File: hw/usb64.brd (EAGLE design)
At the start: 68.6 x 62.5 mm, 22 parts

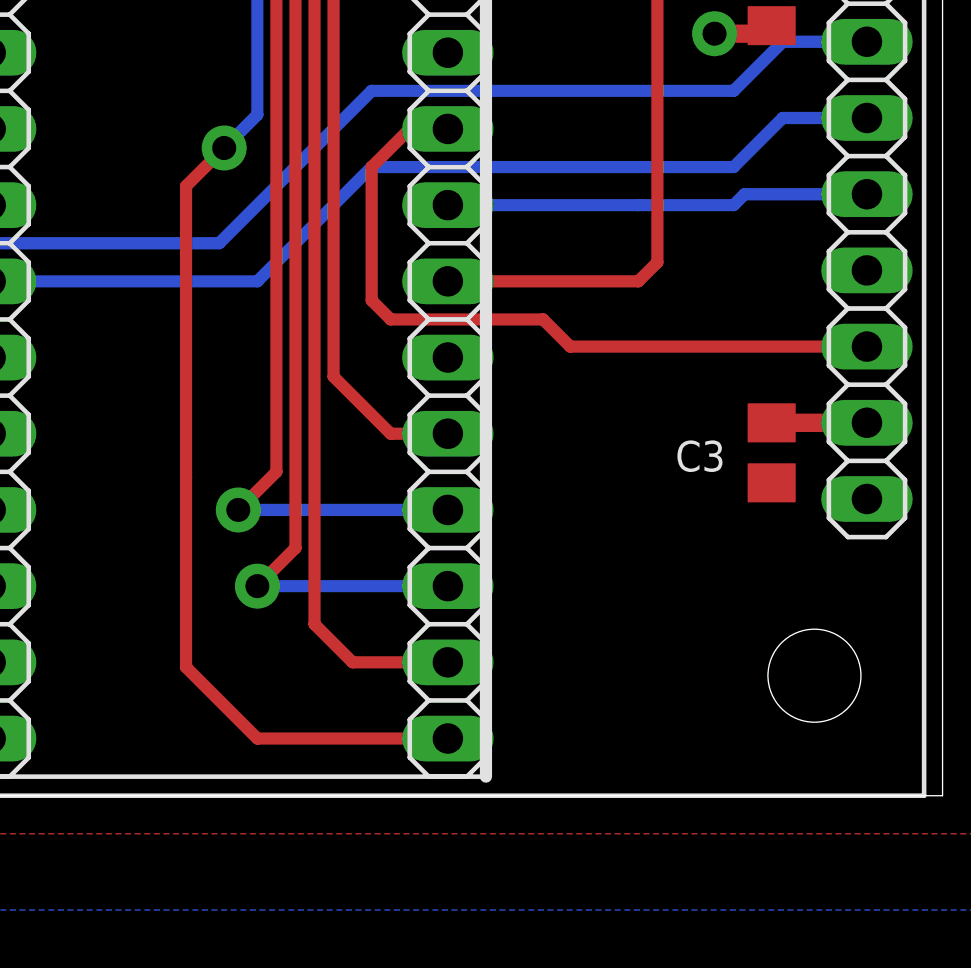
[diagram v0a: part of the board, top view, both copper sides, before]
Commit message: hw: Add 100pF filtering capacitors
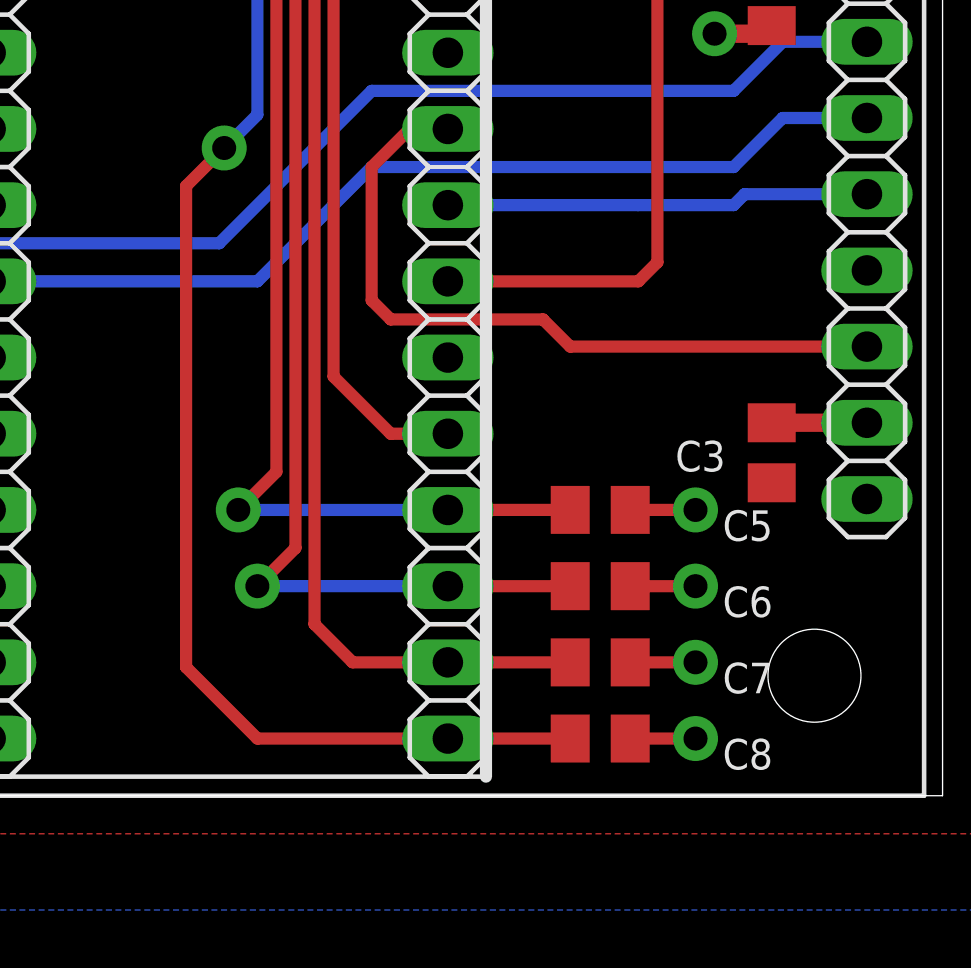
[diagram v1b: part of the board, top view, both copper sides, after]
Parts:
- added C5, C6, C7, C8: 100p, rcl:C0805K
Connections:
- net GND: now also C5.2, C6.2, C7.2, C8.2
- net N64_1: now also C5.1
- net N64_2: now also C6.1
- net N64_3: now also C7.1
- net N64_4: now also C8.1
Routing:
- net GND: track 26.6 -> 35.3 mm, vias 5 -> 9
- net N64_4: track 62.6 -> 66.7 mm
- net N64_3: track 62.9 -> 67.0 mm
- net N64_2: track 71.0 -> 75.1 mm
- net N64_1: track 76.3 -> 80.4 mm
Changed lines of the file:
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@@
 <attribute name="PURCHASE-URL" value="https://pricing.snapeda.com/search/part/USB-A1HSW6/?ref=eda" x="22.225" y="4.445" size="1.778" layer="27" display="off"/>
+</element>
+<element name="C5" library="rcl" library_urn="urn:adsk.eagle:library:334" package="C0805K" package3d_urn="urn:adsk.eagle:package:23681/2" value="100p" x="57.15" y="9.525" smashed="yes">
+<attribute name="NAME" x="61.23" y="8.495" size="1.016" layer="25"/>
+<attribute name="POPULARITY" value="52" x="57.15" y="9.525" size="1.778" layer="27" display="off"/>
+<attribute name="SPICEPREFIX" value="C" x="57.15" y="9.525" size="1.778" layer="27" display="off"/>
+</element>
+<element name="C6" library="rcl" library_urn="urn:adsk.eagle:library:334" package="C0805K" package3d_urn="urn:adsk.eagle:package:23681/2" value="100p" x="57.15" y="6.985" smashed="yes">
+<attribute name="NAME" x="61.23" y="5.955" size="1.016" layer="25"/>
+<attribute name="POPULARITY" value="52" x="57.15" y="6.985" size="1.778" layer="27" display="off"/>
+<attribute name="SPICEPREFIX" value="C" x="57.15" y="6.985" size="1.778" layer="27" display="off"/>
+</element>
+<element name="C7" library="rcl" library_urn="urn:adsk.eagle:library:334" package="C0805K" package3d_urn="urn:adsk.eagle:package:23681/2" value="100p" x="57.15" y="4.445" smashed="yes">
+<attribute name="NAME" x="61.23" y="3.415" size="1.016" layer="25"/>
+<attribute name="POPULARITY" value="52" x="57.15" y="4.445" size="1.778" layer="27" display="off"/>
+<attribute name="SPICEPREFIX" value="C" x="57.15" y="4.445" size="1.778" layer="27" display="off"/>
+</element>
+<element name="C8" library="rcl" library_urn="urn:adsk.eagle:library:334" package="C0805K" package3d_urn="urn:adsk.eagle:package:23681/2" value="100p" x="57.15" y="1.905" smashed="yes">
+<attribute name="NAME" x="61.23" y="0.875" size="1.016" layer="25"/>
+<attribute name="POPULARITY" value="52" x="57.15" y="1.905" size="1.778" layer="27" display="off"/>
+<attribute name="SPICEPREFIX" value="C" x="57.15" y="1.905" size="1.778" layer="27" display="off"/>
 </element>
 </elements>
@@
 <vertex x="78.74" y="72.39"/>
 </polygon>
+<contactref element="C6" pad="2"/>
+<contactref element="C7" pad="2"/>
+<contactref element="C8" pad="2"/>
+<contactref element="C5" pad="2"/>
+<wire x1="58.15" y1="9.525" x2="60.325" y2="9.525" width="0.4064" layer="1"/>
+<via x="60.325" y="9.525" extent="1-16" drill="0.8" diameter="1.5"/>
+<wire x1="58.15" y1="6.985" x2="60.325" y2="6.985" width="0.4064" layer="1"/>
+<via x="60.325" y="6.985" extent="1-16" drill="0.8" diameter="1.5"/>
+<wire x1="58.15" y1="4.445" x2="60.325" y2="4.445" width="0.4064" layer="1"/>
+<via x="60.325" y="4.445" extent="1-16" drill="0.8" diameter="1.5"/>
+<wire x1="58.15" y1="1.905" x2="60.325" y2="1.905" width="0.4064" layer="1"/>
+<via x="60.325" y="1.905" extent="1-16" drill="0.8" diameter="1.5"/>
 </signal>
 <signal name="N64_1">
@@
 <wire x1="6.35" y1="38.735" x2="24.765" y2="38.735" width="0.4064" layer="1"/>
 <wire x1="34.925" y1="28.575" x2="45.085" y2="28.575" width="0.4064" layer="1"/>
+<contactref element="C5" pad="1"/>
+<wire x1="56.15" y1="9.525" x2="52.07" y2="9.525" width="0.4064" layer="1"/>
 </signal>
 <signal name="N64_SENSE">
@@
 <via x="44.6144" y="21.59" extent="1-16" drill="0.8" diameter="1.5"/>
 <wire x1="44.6144" y1="21.59" x2="43.3444" y2="20.32" width="0.4064" layer="1"/>
-<wire x1="43.3444" y1="20.32" x2="43.3444" y2="10.61795625" width="0.4064" layer="1"/>
-<wire x1="43.3444" y1="10.61795625" x2="43.3444" y2="4.2806" width="0.4064" layer="1"/>
+<wire x1="43.3444" y1="20.32" x2="43.3444" y2="4.2806" width="0.4064" layer="1"/>
 <wire x1="43.3444" y1="4.2806" x2="45.72" y2="1.905" width="0.4064" layer="1"/>
 <wire x1="45.72" y1="1.905" x2="52.07" y2="1.905" width="0.4064" layer="1"/>
 <wire x1="45.72" y1="36.195" x2="45.72" y2="22.6956" width="0.4064" layer="16"/>
+<contactref element="C8" pad="1"/>
+<wire x1="52.07" y1="1.905" x2="56.15" y2="1.905" width="0.4064" layer="1"/>
 </signal>
 <signal name="N64_3">
@@
 <wire x1="25.87973125" y1="40.005" x2="32.22973125" y2="33.655" width="0.4064" layer="1"/>
 <wire x1="32.22973125" y1="33.655" x2="45.7962" y2="33.655" width="0.4064" layer="1"/>
+<contactref element="C7" pad="1"/>
+<wire x1="52.07" y1="4.445" x2="56.15" y2="4.445" width="0.4064" layer="1"/>
 </signal>
 <signal name="N64_2">
@@
 <wire x1="15.24" y1="39.37" x2="25.4" y2="39.37" width="0.4064" layer="1"/>
 <wire x1="33.655" y1="31.115" x2="45.72" y2="31.115" width="0.4064" layer="1"/>
+<contactref element="C6" pad="1"/>
+<wire x1="52.07" y1="6.985" x2="56.15" y2="6.985" width="0.4064" layer="1"/>
 </signal>
 <signal name="+3V3">
